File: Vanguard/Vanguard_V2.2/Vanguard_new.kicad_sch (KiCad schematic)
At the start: 72 parts, among them J1 USB_C, J2 Conn_02x03_Pin, J3 Micro_SD_Card_Det1, J4 STARBOARD_SERVO, J5 PORTSIDE_SERVO, J6 Conn_01x02_Pin, Q1 BSS138, Q2 BSS138, Q3 BSS138, Q4 BSS138, U1 ATSAMD11D14A-M, U2 ATmega4809-A, U3 AT25DF641A-SH-T, U4 AP2112K-3.3, U5 MPM3610AGQV-P, U6 BNO086, U7 TXB0104D, U8 TPS61092, Y1 32.768kHz

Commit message: PCB
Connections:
- net GND: now also U8.17 (PAD)
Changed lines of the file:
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@@
 	(wire
 		(pts
+			(xy 386.08 185.42) (xy 386.08 182.88)
+		)
+		(stroke
+			(width 0)
+			(type default)
+		)
+	)
+	(wire
+		(pts
 			(xy 398.78 154.94) (xy 407.67 154.94)
 		)
@@
 					(unit 1)
 				)
+			)
+		)
+	)
+	(symbol
+		(lib_id "power:GND")
+		(at 386.08 185.42 0)
+		(unit 1)
+		(exclude_from_sim no)
+		(in_bom yes)
+		(on_board yes)
+		(dnp no)
+		(fields_autoplaced yes)
+		(property "Reference" "#PWR072"
+			(at 386.08 191.77 0)
+			(effects
+				(font
+					(size 1.27 1.27)
+				)
+				(hide yes)
+			)
+		)
+		(property "Value" "GND"
+			(at 386.08 190.5 0)
+			(effects
+				(font
+					(size 1.27 1.27)
+				)
+			)
+		)
+		(property "Footprint" ""
+			(at 386.08 185.42 0)
+			(effects
+				(font
+					(size 1.27 1.27)
+				)
+				(hide yes)
+			)
+		)
+		(property "Datasheet" ""
+			(at 386.08 185.42 0)
+			(effects
+				(font
+					(size 1.27 1.27)
+				)
+				(hide yes)
+			)
+		)
+		(property "Description" "Power symbol creates a global label with name \"GND\" , ground"
+			(at 386.08 185.42 0)
+			(effects
+				(font
+					(size 1.27 1.27)
+				)
+				(hide yes)
+			)
+		)
+		(pin "1"
+		)
+		(instances
+			(project ""
+				(path "/972fbf12-2dcd-4fdf-b1c9-8a2880c46640"
+					(reference "#PWR072")
+					(unit 1)
+				)

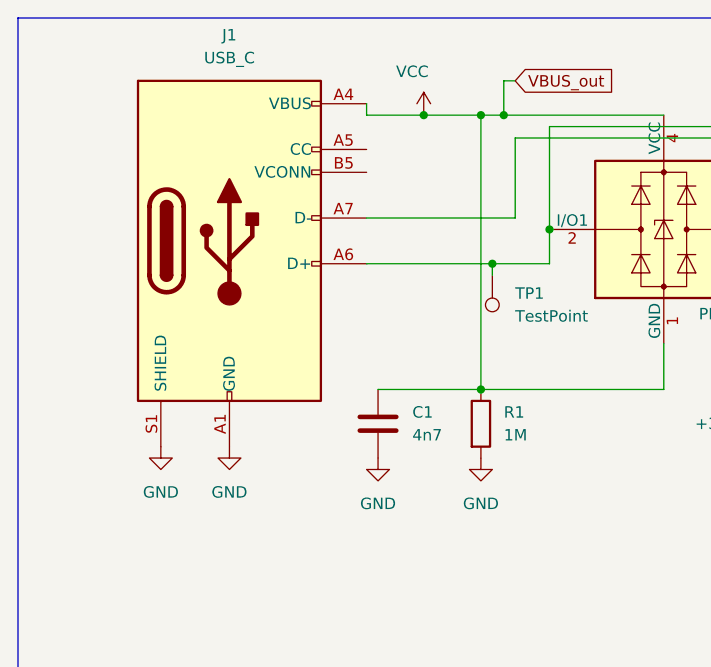
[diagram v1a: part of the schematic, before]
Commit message: REPLACEDthe  USB_ and added new connections
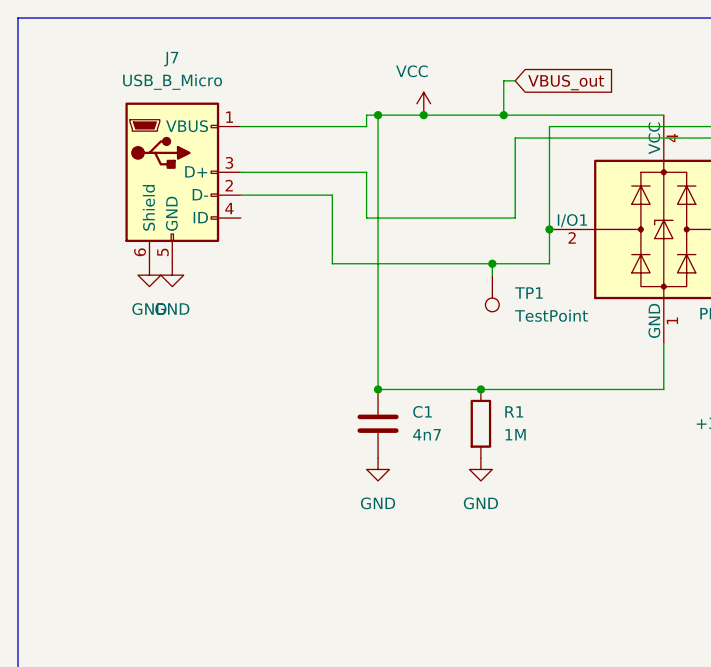
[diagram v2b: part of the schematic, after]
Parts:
- removed J1: USB_C, Connector_USB:USB_C_Plug_Molex_105444, symbol Connector:USB_C_Plug_USB2.0
- added J7: USB_B_Micro, Connector_USB:USB_Micro-B_Wuerth_614105150721_Vertical_CircularHoles, symbol Connector:USB_B_Micro
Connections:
- net GND: now also J7.5 (GND), J7.6 (Shield)
- net VCC: now also J7.1 (VBUS)
- net at D1.2 (I/O1), TP1.1, U1.22 (PA25): now also J7.2 (D-)
- net at D1.3 (I/O2), TP2.1, U1.21 (PA24): now also J7.3 (D+)

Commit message: schematic + pcb changes
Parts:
- removed U5: MPM3610AGQV-P, MPM3610AGQV_P:CONV_MPM3620AGQV-P, symbol MPM3610AGQV-P:MPM3610AGQV-P
- added U9: MPM3610AGQV-P, MPM3610AGQV_P:CONV_MPM3620AGQV-P, symbol MPM3610AGQV-P:MPM3610AGQV-P
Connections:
- net GND: now also U9.12 (PGND), U9.13 (PGND), U9.14 (PGND), U9.3 (AGND)
- net VCC: now also U9.2 (VCC)
- net at C4.1, R14.1: now also U9.16 (IN)
- net at R14.2: now also U9.17 (EN)
- net at R15.2, R16.1: now also U9.1 (FB)
- net at C5.1, R15.1, U4.1 (VIN)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: now also U9.20 (OUT), U9.7 (OUT), U9.8 (OUT), U9.9 (OUT)
- new net: U9.19 (SW), U9.4 (SW), U9.5 (SW), U9.6 (SW)

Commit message: pcb finished
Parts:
- removed J7: USB_B_Micro, Connector_USB:USB_Micro-B_Wuerth_614105150721_Vertical_CircularHoles, symbol Connector:USB_B_Micro
- added P1: USB_C_Plug_USB2.0, Connector_USB:USB_C_Plug_Molex_105444, symbol Connector:USB_C_Plug_USB2.0
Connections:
- net GND: now also P1.A1 (GND), P1.A12 (GND), P1.B1 (GND), P1.B12 (GND), P1.S1 (SHIELD)
- net VCC: now also P1.A4 (VBUS), P1.A9 (VBUS), P1.B4 (VBUS), P1.B9 (VBUS)
- net at D1.2 (I/O1), TP1.1, U1.22 (PA25): now also P1.A6 (D+)
- net at D1.3 (I/O2), TP2.1, U1.21 (PA24): now also P1.A7 (D-)
- no-connect marks 0 -> 1

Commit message: small changes
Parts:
- removed P1: USB_C_Plug_USB2.0, Connector_USB:USB_C_Plug_Molex_105444, symbol Connector:USB_C_Plug_USB2.0
- C7: value 0.1uF -> 0u1F
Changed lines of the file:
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@@
 			)
 		)
-		(property "Value" "0.1uF"
+		(property "Value" "0u1F"
 			(at 121.158 170.688 90)
 			(effects
@@
 					(unit 1)
 				)
-			)
-		)
-	)
-	(symbol
-		(lib_id "Connector:USB_C_Plug_USB2.0")
-		(at 33.02 40.64 0)
-		(unit 1)
-		(exclude_from_sim no)
-		(in_bom yes)
-		(on_board yes)
-		(dnp no)
-		(fields_autoplaced yes)
-		(property "Reference" "P1"
-			(at 33.02 17.78 0)
-			(effects
-				(font
-					(size 1.27 1.27)
-				)
-			)
-		)
-		(property "Value" "USB_C_Plug_USB2.0"
-			(at 33.02 20.32 0)
-			(effects
-				(font
-					(size 1.27 1.27)
-				)
-			)
-		)
-		(property "Footprint" "Connector_USB:USB_C_Plug_Molex_105444"
-			(at 36.83 40.64 0)
-			(effects
-				(font
-					(size 1.27 1.27)
-				)
-				(hide yes)
-			)
-		)
-		(property "Datasheet" "https://www.usb.org/sites/default/files/documents/usb_type-c.zip"
-			(at 36.83 40.64 0)
-			(effects
-				(font
-					(size 1.27 1.27)
-				)
-				(hide yes)
-			)
-		)
-		(property "Description" "USB 2.0-only Type-C Plug connector"
-			(at 33.02 40.64 0)
-			(effects
-				(font
-					(size 1.27 1.27)
-				)
-				(hide yes)
-			)
-		)
-		(pin "B5"
-		)
-		(pin "A5"
-		)
-		(pin "B1"
-		)
-		(pin "B9"
-		)
-		(pin "S1"
-		)
-		(pin "A1"
-		)
-		(pin "A12"
-		)
-		(pin "A4"
-		)
-		(pin "B4"
-		)
-		(pin "A7"
-		)
-		(pin "B12"
-		)
-		(pin "A6"
-		)
-		(pin "A9"
-		)
-		(instances
-			(project ""
-				(path "/972fbf12-2dcd-4fdf-b1c9-8a2880c46640"
-					(reference "P1")
-					(unit 1)
-				)

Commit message: made changes in the names of the resistor and caps, made changes in the usb c wiring, added a temperature sensor and added a label to the microcontroller
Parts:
- added J1: USB_C_Receptacle_USB2.0_16P, Connector_USB:USB_C_Receptacle_Amphenol_12401548E4-2A, symbol Connector:USB_C_Receptacle_USB2.0_16P
- added R31, R32: 5k1, symbol Device:R
- added U5: BD1020HFV, Package_TO_SOT_SMD:HVSOF5, symbol Sensor_Temperature:BD1020HFV
- C10: value 100 uF -> 100u
- C2, C3: value 22pF -> 2p2
- C8: value 10 uF -> 10u
- C9: value 2.2uF -> 2u2
- L1: value 6.8 uH -> 6u8
- R19, R20: value 4.7k -> 4k7
- R21, R22: value 2.2k -> 2k2
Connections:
- net +3.3V: now also U5.4 (VDD)
- net GND: now also J1.A1 (GND), J1.A12 (GND), J1.B1 (GND), J1.B12 (GND), J1.S1 (SHIELD), R31.2, R32.2, U5.2 (PG), U5.5 (GND)
- net VCC: now also J1.A4 (VBUS), J1.A9 (VBUS), J1.B4 (VBUS), J1.B9 (VBUS)
- net at D1.2 (I/O1), TP1.1, U1.22 (PA25): now also J1.A6 (D+), J1.B6 (D+)
- net at D1.3 (I/O2), TP2.1, U1.21 (PA24): now also J1.A7 (D-), J1.B7 (D-)
- net TEMP_SENSOR: now reaches U2.3 (PA7)
- net TEMP_SENSOR: now also U5.3 (OUT)
- new net: J1.A5 (CC1), R31.1
- new net: J1.B5 (CC2), R32.1

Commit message: Assigned footprints, added dnps and changed some connections in tx0 and rx0 pins
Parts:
- C10: footprint Capacitor_SMD:C_0201_0603Metric -> Capacitor_SMD:CP_Elec_6.3x5.4
- R31, R32: footprint (none) -> Resistor_SMD:R_0402_1005Metric
- U3: footprint AT25DF641A-SH-T:SOIC127P798X216-8N -> Package_SO:SOIC-8_3.9x4.9mm_P1.27mm
- U6: footprint BNO086:IC_BNO086 -> Package_LGA:LGA-28_5.2x3.8mm_P0.5mm
- U9: footprint MPM3610AGQV_P:CONV_MPM3620AGQV-P -> Package_DFN_QFN:QFN-16-1EP_3x3mm_P0.5mm_EP1.7x1.7mm
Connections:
- net RX_UPDI: no longer D4.2 (A), Q1.2 (S), R5.2, R6.2, R8.1, U1.11 (PA14)
- net at D3.1 (K), Q2.2 (S), R10.2: now also U1.16 (PA23); no longer U1.15 (PA22)
- net at D2.1 (K), Q3.2 (S), R9.2: now also U1.15 (PA22); no longer U1.16 (PA23)
- new net TX_UPDI: D4.2 (A), Q1.2 (S), R5.2, R6.2, R8.1, U1.11 (PA14)
- no-connect marks 1 -> 49

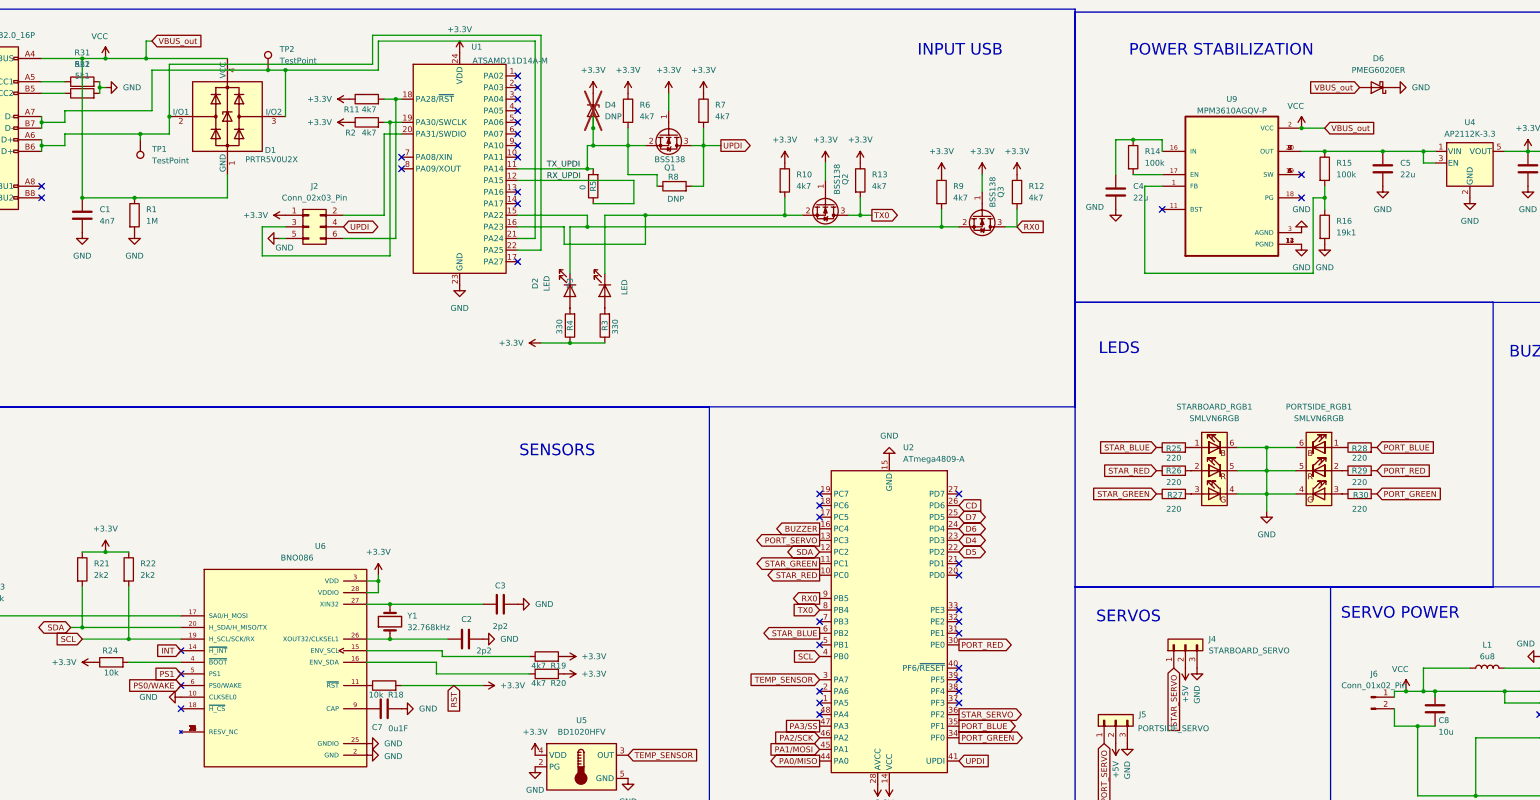
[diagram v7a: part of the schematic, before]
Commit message: Ran ERC and Assigned  VBUS label
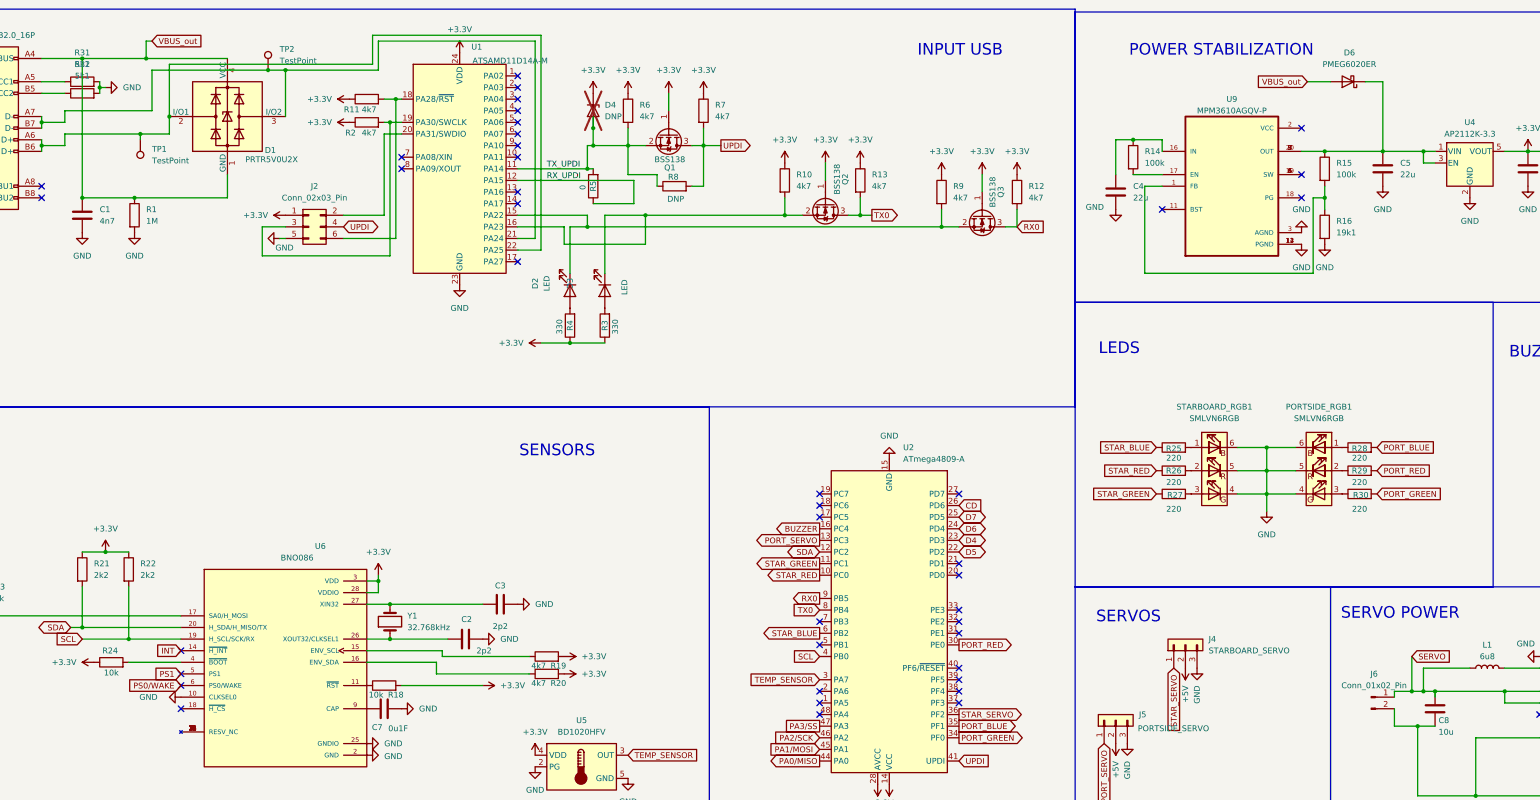
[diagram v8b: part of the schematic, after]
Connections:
- net GND: no longer D6.1 (K)
- net at C5.1, R15.1, U4.1 (VIN)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: now also D6.1 (K)
- net VCC renamed VBUS_out
- net VBUS_out: no longer C8.1, J6.1 (Pin_1), L1.1, U8.11 (EN), U8.8 (VBAT), U9.2 (VCC)
- new net SERVO: C8.1, J6.1 (Pin_1), L1.1, U8.11 (EN), U8.8 (VBAT)
- no-connect marks 49 -> 50
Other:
- moved on the sheet: D6
